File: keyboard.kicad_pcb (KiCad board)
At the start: 2 copper layers, 304.8 x 133.3 mm, 219 parts, among them J1 USB_C_Receptacle_USB2.0, J2 AVR-ISP-6, SW1 SW_Push, SW10 SW_Push, SW11 SW_Push, SW12 SW_Push, SW13 SW_Push, SW14 SW_Push, SW15 SW_Push, SW16 SW_Push, SW17 SW_Push, SW18 SW_Push, SW19 SW_Push, SW2 SW_Push, SW20 SW_Push, SW21 SW_Push, SW22 SW_Push, SW23 SW_Push, SW24 SW_Push, SW25 SW_Push, SW26 SW_Push, SW27 SW_Push, SW28 SW_Push, SW29 SW_Push, SW3 SW_Push, SW30 SW_Push, SW31 SW_Push, SW32 SW_Push, SW33 SW_Push, SW34 SW_Push, SW35 SW_Push, SW36 SW_Push, SW37 SW_Push, SW38 SW_Push, SW39 SW_Push, SW4 SW_Push, SW40 SW_Push, SW41 SW_Push, SW42 SW_Push, SW43 SW_Push, SW44 SW_Push, SW45 SW_Push, SW46 SW_Push, SW47 SW_Push, SW48 SW_Push, SW49 SW_Push, SW5 SW_Push, SW50 SW_Push, SW51 SW_Push, SW52 SW_Push, SW53 SW_Push, SW54 SW_Push, SW55 SW_Push, SW56 SW_Push, SW57 SW_Push, SW58 SW_Push, SW59 SW_Push, SW6 SW_Push, SW60 SW_Push, SW61 SW_Push, SW62 SW_Push, SW63 SW_Push, SW64 SW_Push, SW65 SW_Push, SW66 SW_Push, SW67 SW_Push, SW68 SW_Push, SW69 SW_Push, SW7 SW_Push, SW70 SW_Push, SW71 SW_Push, SW72 SW_Push, SW73 SW_Push, SW74 SW_Push, SW75 SW_Push, SW76 SW_Push, SW77 SW_Push, SW78 SW_Push, SW79 SW_Push, SW8 SW_Push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

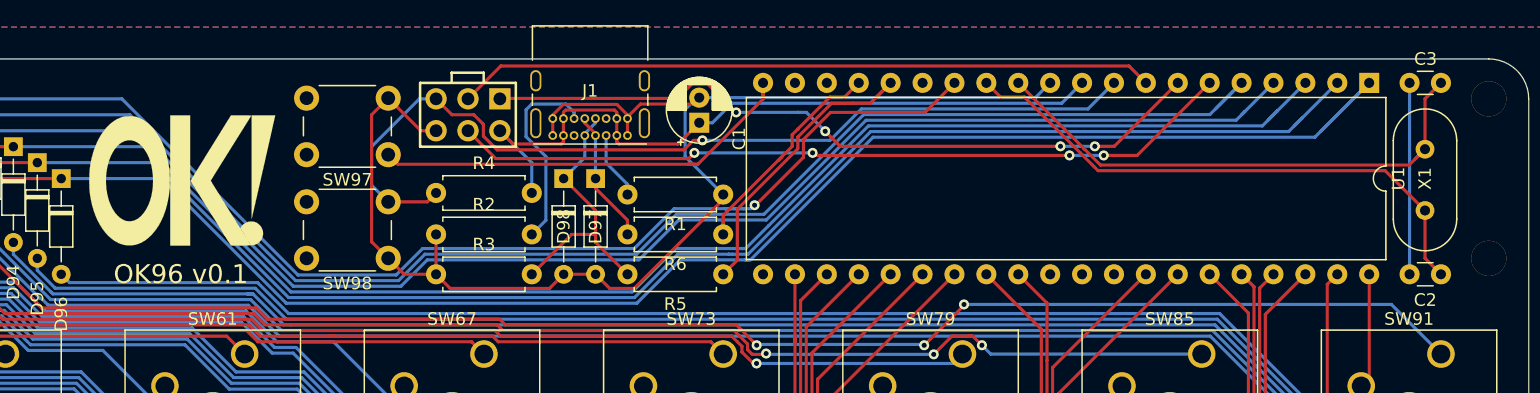
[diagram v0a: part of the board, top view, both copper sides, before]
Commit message: minor silkscreen fixes, v0.1.1
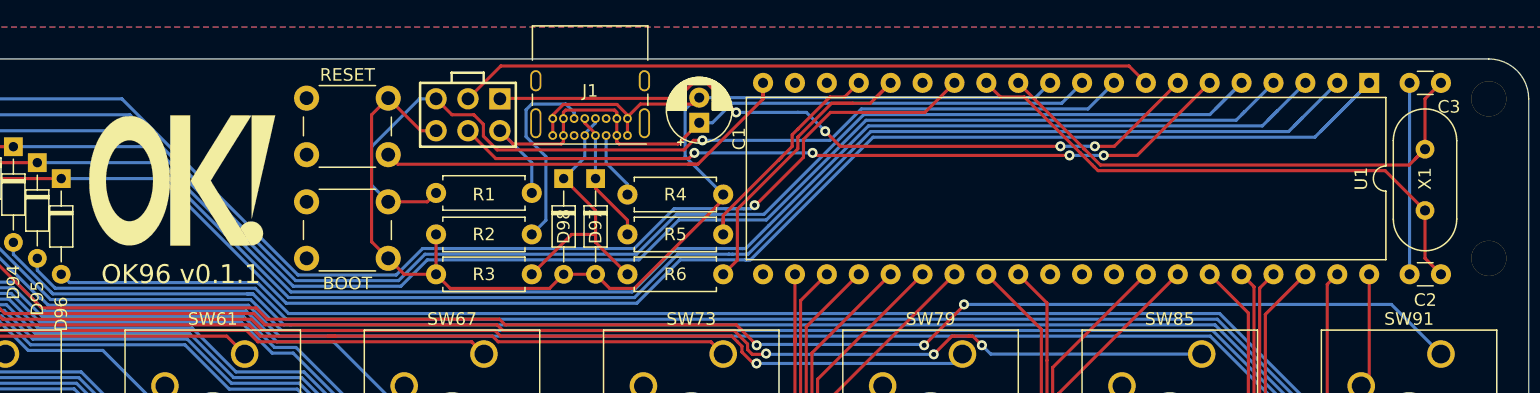
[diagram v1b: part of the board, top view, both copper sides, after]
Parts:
- renumbered SW98 to BOOT, R4 to R1, R1 to R4, R6 to R5, R5 to R6, SW97 to RESET
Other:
- board text added: "OK96 v0.1.1"
- board text removed: "OK96 v0.1"
